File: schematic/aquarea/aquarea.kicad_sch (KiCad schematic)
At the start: 29 parts, among them J1 RC_CABLE, J2 HP_CABLE, J3 ESP_PROG, Q1 BC847, Q2 BC847, Q3 BC847, Q4 BC847, Q5 BC847, Q6 BC847, Q7 BC847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

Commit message: Update schematic andpcb after tests; add bom and gerbers
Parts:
- removed D1: D_Schottky_Small, Diode_SMD:D_MiniMELF_Handsoldering, symbol Device:D_Schottky_Small
- removed Q4: BC847, Package_TO_SOT_SMD:SOT-23, symbol Transistor_BJT:BC847
- added Q4: BC857, Package_TO_SOT_SMD:SOT-23, symbol Transistor_BJT:BC857
- added SW2: Reset, Resistor_SMD:R_0508_1220Metric, symbol Switch:SW_Push
- R5: value 10k -> 20k
- renumbered D3 to D1
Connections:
- net +3V3: now also C2.1, U2.2 (VO)
- net ESP_RX: now also U1.7 (GPIO13)
- net ESP_TX: no longer U1.7 (GPIO13)
- net at R8.1: now also Q4.1 (B)
- net at Q6.1 (B): now also Q4.3 (C)
- net at R7.1: now also Q4.2 (E)
- net at R3.1: now also SW2.1; no longer U1.1 (~{RST})
- new net: SW2.2, U1.1 (~{RST})
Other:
- moved on the sheet: D1, J3, R11, R12, R3, SW1, U1

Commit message: Update schematic
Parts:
- removed SW2: Reset, Resistor_SMD:R_0508_1220Metric, symbol Switch:SW_Push
- added SW2: RESET, Button_Switch_SMD:SW_Push_SPST_NO_Alps_SKRK, symbol Switch:SW_Push_Open
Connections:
- net at R3.1: now also SW2.1 (A)
- net at U1.1 (~{RST}): now also SW2.2 (B)
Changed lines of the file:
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@@
+	)
+	(symbol
+		(lib_id "Switch:SW_Push_Open")
+		(at 92.71 26.67 0)
+		(unit 1)
+		(exclude_from_sim no)
+		(in_bom yes)
+		(on_board yes)
+		(dnp no)
+		(fields_autoplaced yes)
+		(property "Reference" "SW2"
+			(at 92.71 20.32 0)
+			(effects
+				(font
+					(size 1.27 1.27)
+				)
+			)
+		)
+		(property "Value" "RESET"
+			(at 92.71 22.86 0)
+			(effects
+				(font
+					(size 1.27 1.27)
+				)
+			)
+		)
+		(property "Footprint" "Button_Switch_SMD:SW_Push_SPST_NO_Alps_SKRK"
+			(at 92.71 21.59 0)
+			(effects
+				(font
+					(size 1.27 1.27)
+				)
+				(hide yes)
+			)
+		)
+		(property "Datasheet" "~"
+			(at 92.71 21.59 0)
+			(effects
+				(font
+					(size 1.27 1.27)
+				)
+				(hide yes)
+			)
+		)
+		(property "Description" "Push button switch, push-to-open, generic, two pins"
+			(at 92.71 26.67 0)
+			(effects
+				(font
+					(size 1.27 1.27)
+				)
+				(hide yes)
+			)
+		)
+		(pin "1"
+		)
+		(pin "2"
+		)
+		(instances
+			(project ""
+				(path "/ea22a014-a242-4a47-8f14-43aa24d75b8c"
+					(reference "SW2")
+					(unit 1)
+				)
+			)
+		)
 	)
 	(symbol
@@
 					(unit 1)
 				)
-			)
-		)
-	)
-	(symbol
-		(lib_id "Switch:SW_Push")
-		(at 92.71 26.67 0)
-		(unit 1)
-		(exclude_from_sim no)
-		(in_bom yes)
-		(on_board yes)
-		(dnp no)
-		(property "Reference" "SW2"
-			(at 92.456 20.828 0)
-			(effects
-				(font
-					(size 1.27 1.27)
-				)
-			)
-		)
-		(property "Value" "Reset"
-			(at 92.71 22.606 0)
-			(effects
-				(font
-					(size 1.27 1.27)
-				)
-			)
-		)
-		(property "Footprint" "Resistor_SMD:R_0508_1220Metric"
-			(at 92.71 21.59 0)
-			(effects
-				(font
-					(size 1.27 1.27)
-				)
-				(hide yes)
-			)
-		)
-		(property "Datasheet" "~"
-			(at 92.71 21.59 0)
-			(effects
-				(font
-					(size 1.27 1.27)
-				)
-				(hide yes)
-			)
-		)
-		(property "Description" "Push button switch, generic, two pins"
-			(at 92.71 26.67 0)
-			(effects
-				(font
-					(size 1.27 1.27)
-				)
-				(hide yes)
-			)
-		)
-		(pin "1"
-		)
-		(pin "2"
-		)
-		(instances
-			(project "aquarea"
-				(path "/ea22a014-a242-4a47-8f14-43aa24d75b8c"
-					(reference "SW2")
-					(unit 1)
-				)

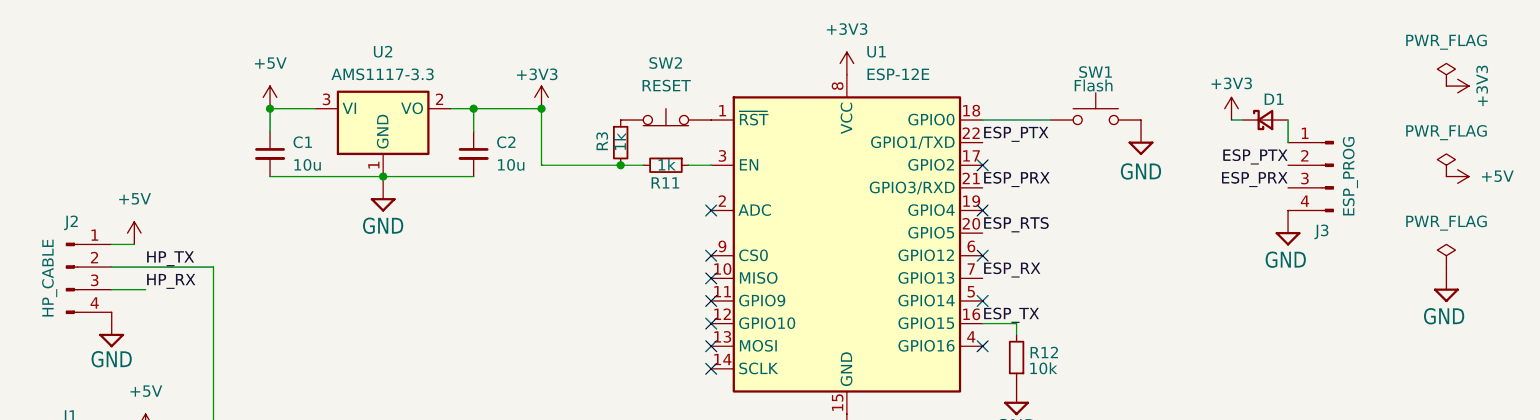
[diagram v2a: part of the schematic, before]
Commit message: Add proper reset handling and optimize design adround antenna
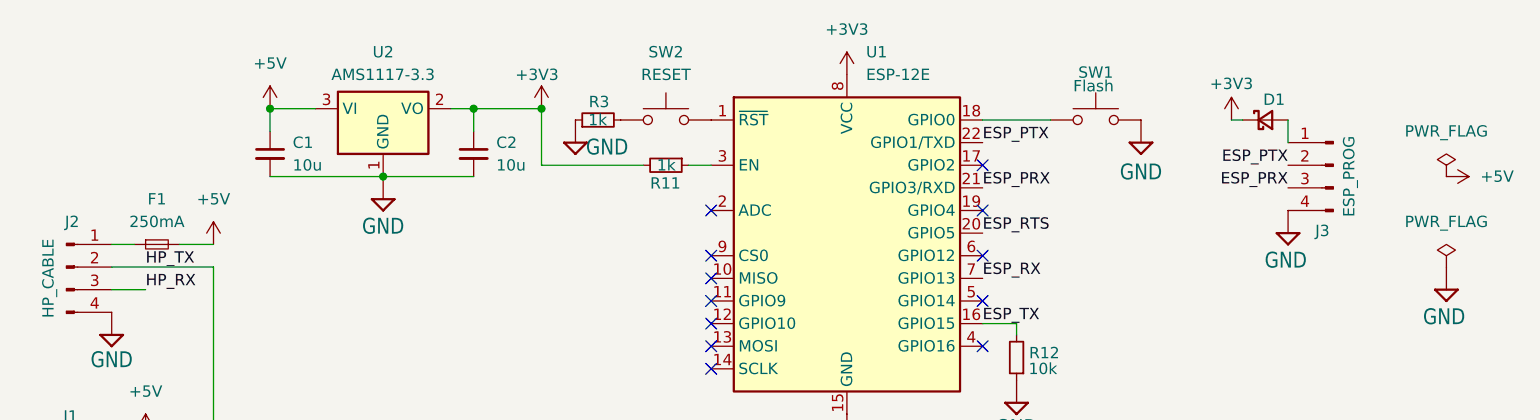
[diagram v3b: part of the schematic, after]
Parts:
- added F1: 250mA, Fuse:Fuse_1812_4532Metric, symbol Device:Fuse_Small
- SW2: symbol Switch:SW_Push_Open -> Switch:SW_Push
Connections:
- net +3V3: no longer R3.2
- net +5V: now also F1.2; no longer J2.1 (Pin_1)
- net GND: now also R3.1
- net at SW2.1: now also R3.2; no longer R3.1
- new net: F1.1, J2.1 (Pin_1)
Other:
- moved on the sheet: R3, SW2
